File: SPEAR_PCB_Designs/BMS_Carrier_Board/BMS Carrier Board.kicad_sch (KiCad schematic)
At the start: 3 parts, among them SW1 SW_SPDT_321, U1 74LV1T08GW

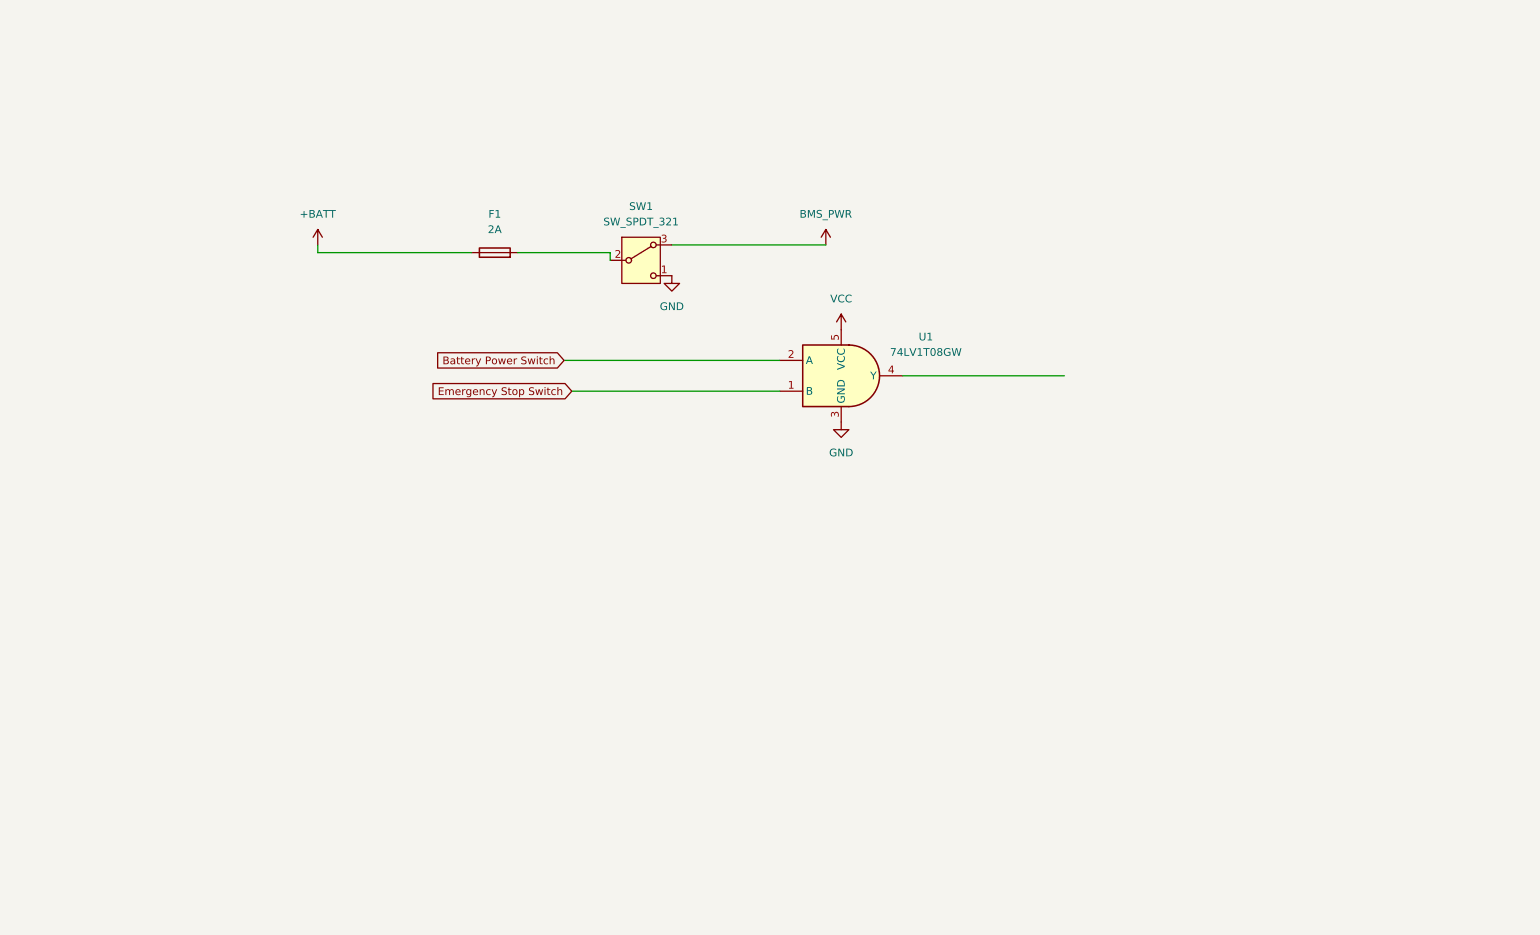
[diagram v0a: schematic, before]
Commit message: created BMS board schematic
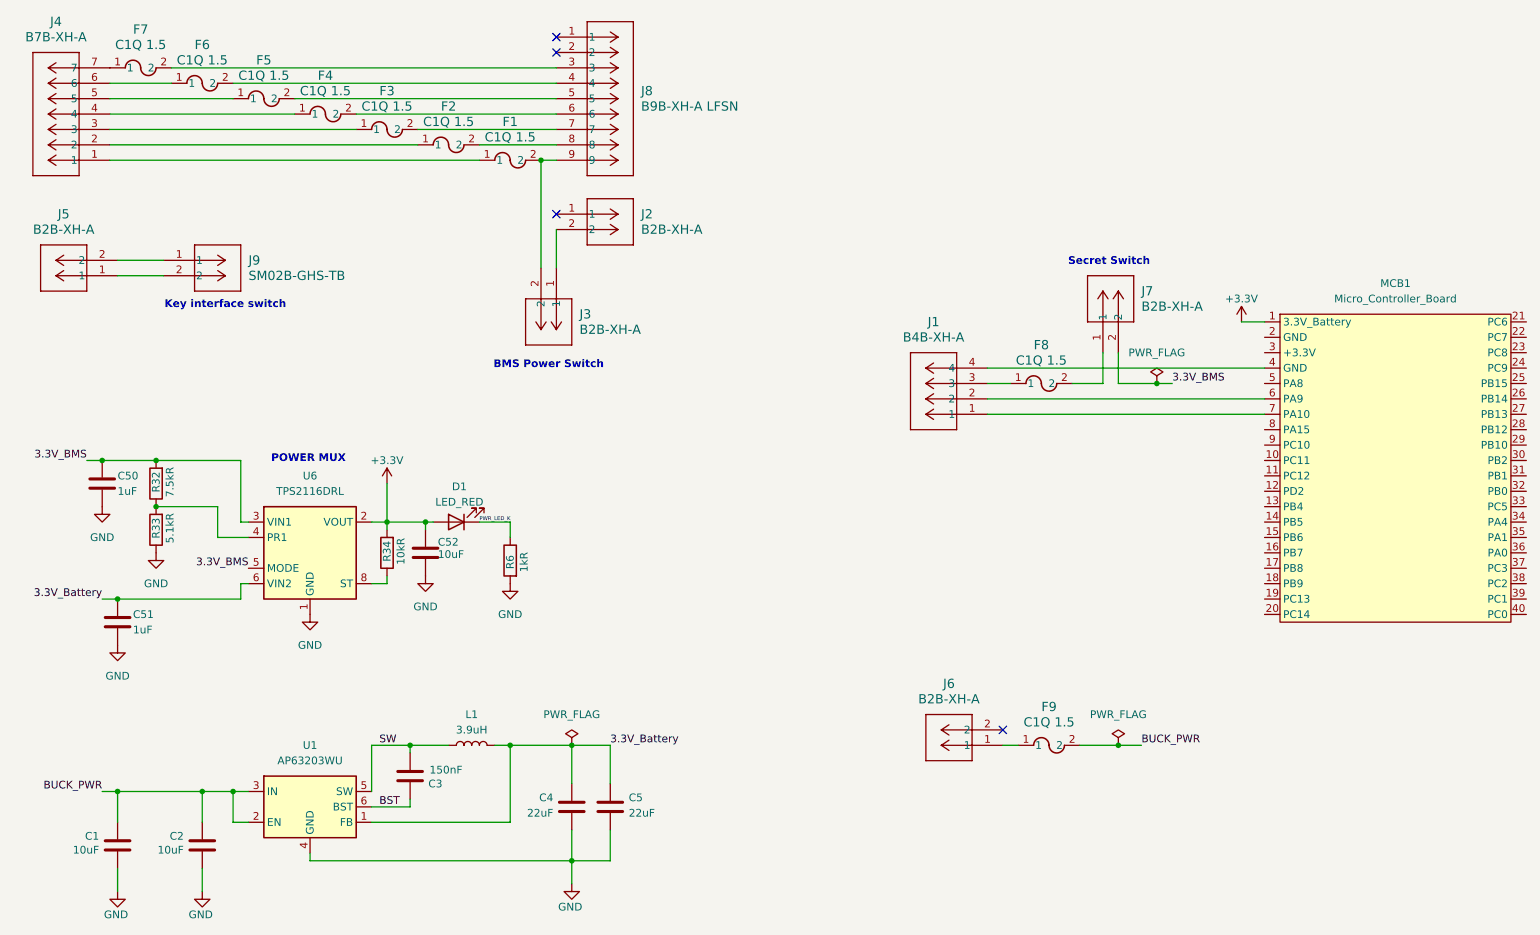
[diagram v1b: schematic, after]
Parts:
- removed F1: 2A, Fuse:Fuse_0402_1005Metric, symbol Device:Fuse
- removed SW1: SW_SPDT_321, symbol Switch:SW_SPDT_321
- removed U1: 74LV1T08GW, Package_TO_SOT_SMD:SOT-353_SC-70-5, symbol 74xx:74LV1T08GW
- added C1, C2: 10uF, SPEAR_MotorControllerCarrier:CAPC3225X270N, symbol Device:C
- added C3: 150nF, SPEAR_MotorControllerCarrier:CAP_CC1206_YAG, symbol Device:C
- added C4, C5: 22uF, SPEAR_MotorControllerCarrier:CAP_C3225X7R1C226M250AC, symbol Device:C
- added C50, C51: 1uF, Capacitor_SMD:C_0402_1005Metric, symbol Device:C
- added C52: 10uF, Capacitor_SMD:C_0603_1608Metric, symbol Device:C
- added D1: LED_RED, LED_SMD:LED_0603_1608Metric, symbol Device:LED
- added F1, F2, F3, F4, F5, F6, F7, F8, F9: C1Q 1.5, C1_BEL, symbol BMS symbols:C1Q_1.5
- added J1: B4B-XH-A, BMS footprints:CONN_B4B-XH-A_JST, symbol BMS symbols:B4B-XH-A
- added J2, J3, J5, J6, J7: B2B-XH-A, CONN_B2B-XH-A_JST, symbol BMS symbols:B2B-XH-A
- added J4: B7B-XH-A, CONN_B7B-XH-A_JST, symbol BMS symbols:B7B-XH-A
- added J8: B9B-XH-A LFSN, CONN_B9B-XH-ALFSN_JST, symbol BMS symbols:B9B-XH-A
- added J9: SM02B-GHS-TB, CONN_SM02B-GHS_JST, symbol BMS symbols:SM02B-GHS-TB
- added L1: 3.9uH, SPEAR_AP63203BuckConverter:L_Wurth_WE-LHMI-1040_L1, symbol Device:L
- added MCB1: Micro_Controller_Board, SPEAR_Boards:Micro_Controller_Board, symbol SPEAR_Boards:Micro_Controller_Board
- added R32: 7.5kR, Resistor_SMD:R_0402_1005Metric, symbol Device:R
- added R33: 5.1kR, Resistor_SMD:R_0402_1005Metric, symbol Device:R
- added R34: 10kR, Resistor_SMD:R_0402_1005Metric, symbol Device:R
- added R6: 1kR, Resistor_SMD:R_0402_1005Metric, symbol Device:R
- added U1: AP63203WU, Package_TO_SOT_SMD:TSOT-23-6, symbol Regulator_Switching:AP63203WU
- added U6: TPS2116DRL, Package_TO_SOT_SMD:SOT-583-8, symbol Power_Management:TPS2116DRL
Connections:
- net GND: now also C1.2, C2.2, C4.2, C5.2, C50.2, C51.2, C52.2, R33.1, R6.2, U1.4 (GND), U6.1 (GND)
- new net: R34.1, U6.8 (ST)
- new net: J2.2, J3.1
- new net: F7.2, J8.3
- new net: F6.2, J8.4
- new net: F5.2, J8.5
- new net: F4.2, J8.6
- new net: F3.2, J8.7
- new net: F2.2, J8.8
- new net: F1.2, J3.2, J8.9
- new net: F1.1, J4.1
- new net: F2.1, J4.2
- new net: F3.1, J4.3
- new net: F4.1, J4.4
- new net: F5.1, J4.5
- new net: F6.1, J4.6
- new net: F7.1, J4.7
- new net: J1.4, MCB1.4 (GND)
- new net: J1.2, MCB1.6 (PA9)
- new net: J1.1, MCB1.7 (PA10)
- new net: R32.1, R33.2, U6.4 (PR1)
- new net: F8.1, J1.3
- new net: J5.1, J9.2
- new net: J5.2, J9.1
- new net: F8.2, J7.1
- new net: F9.1, J6.1
- new net +3.3V: C52.1, D1.2 (A), MCB1.1 (3.3V_Battery), R34.2, U6.2 (VOUT), U6.7 (VOUT)
- new net 3.3V_BMS: C50.1, J7.2, R32.2, U6.3 (VIN1), U6.5 (MODE)
- new net 3.3V_Battery: C4.1, C5.1, C51.1, L1.2, U1.1 (FB), U6.6 (VIN2)
- new net BST: C3.2, U1.6 (BST)
- new net BUCK_PWR: C1.1, C2.1, F9.2, U1.2 (EN), U1.3 (IN)
- new net PWR_LED_K: D1.1 (K), R6.1
- new net SW: C3.1, L1.1, U1.5 (SW)
- no-connect marks 0 -> 4
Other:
- note added: "BMS Power Switch"
- note added: "Key interface switch"
- note added: "POWER MUX"
- note added: "Secret Switch"
